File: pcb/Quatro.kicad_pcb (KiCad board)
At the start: 2 copper layers, 100 x 72.8 mm, 97 parts, among them J1 BATTERY, J2 BATTERY, J3 Conn_01x02, J4 UART1 SH, J5 st-link SH, J6 2.54mm 02x03, J7 2.54mm 02x03, Q1 IRLML6402, Q2 IRFML8244, Q3 BSS138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

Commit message: 再発注用に変更
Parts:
- added R30: 10k, Resistor_SMD:R_0603_1608Metric_Pad0.98x0.95mm_HandSolder, F.Cu at (117.8, 109.3)
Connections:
- C10 pad 1: BUTTON -> +3V3
- C17 pad 1: BUTTON -> +3V3
- C18 pad 1: BUTTON -> +3V3
- C19 pad 1: BUTTON -> +3V3
- C20 pad 1: BUTTON -> +3V3
- C22 pad 1: BUTTON -> +3V3
- C6 pad 1: BUTTON -> +3V3
- C7 pad 1: BUTTON -> +3V3
- R14 pad 1: BUTTON -> +3V3
- SP1 pad 1: BUTTON -> +3V3
- U2 pad 3: BUTTON -> +3V3
- U6 pad 13: BUTTON -> +3V3
- U6 pad 8: BUTTON -> +3V3
- U7 pad 1: BUTTON -> +3V3
- U7 pad 19: BUTTON -> +3V3
- U7 pad 32: BUTTON -> +3V3
- U7 pad 48: BUTTON -> +3V3
- U7 pad 64: BUTTON -> +3V3
- U8 pad 12: BUTTON -> +3V3
- U9 pad 12: BUTTON -> +3V3
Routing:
- net BUTTON: track 289.1 -> 52.1 mm, vias 13 -> 2
- net +3V3: track 0.00 -> 198.1 mm, vias 0 -> 5
- net +5V: track 213.8 -> 123.8 mm
- net +3.3VADC: track 205.2 -> 145.2 mm, vias 4 -> 0
- net Net-(R13-Pad1): track 50.9 -> 3.43 mm
- net GND: track 669.4 -> 626.4 mm, vias 51 -> 36
- net TIM5_CH4_MOTOR_R_IN2: track 31.3 -> 66.4 mm, vias 4 -> 3
- net TIM3_CH1_ENC_L_A: track 44.7 -> 19.7 mm
- net TIM5_CH3_MOTOR_R_IN1: track 27.9 -> 51.8 mm, vias 0 -> 2
- net NRST: track 76.9 -> 54.2 mm, vias 0 -> 3
- net Net-(D7-Pad1): track 55.3 -> 77.9 mm
- net MOTOR_R_OUT1: track 24.5 -> 45.7 mm
- net LED5: track 49.3 -> 29.9 mm
- net LED1: track 64.3 -> 80.9 mm
- net MOTOR_L_OUT1: track 31.4 -> 15.1 mm, vias 1 -> 0
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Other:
- board text added: "2021-12-05"
- board text added: "T.Reiji Quatro"
- board text removed: "2021-11-24"
- board text removed: "Quatro Cheese"

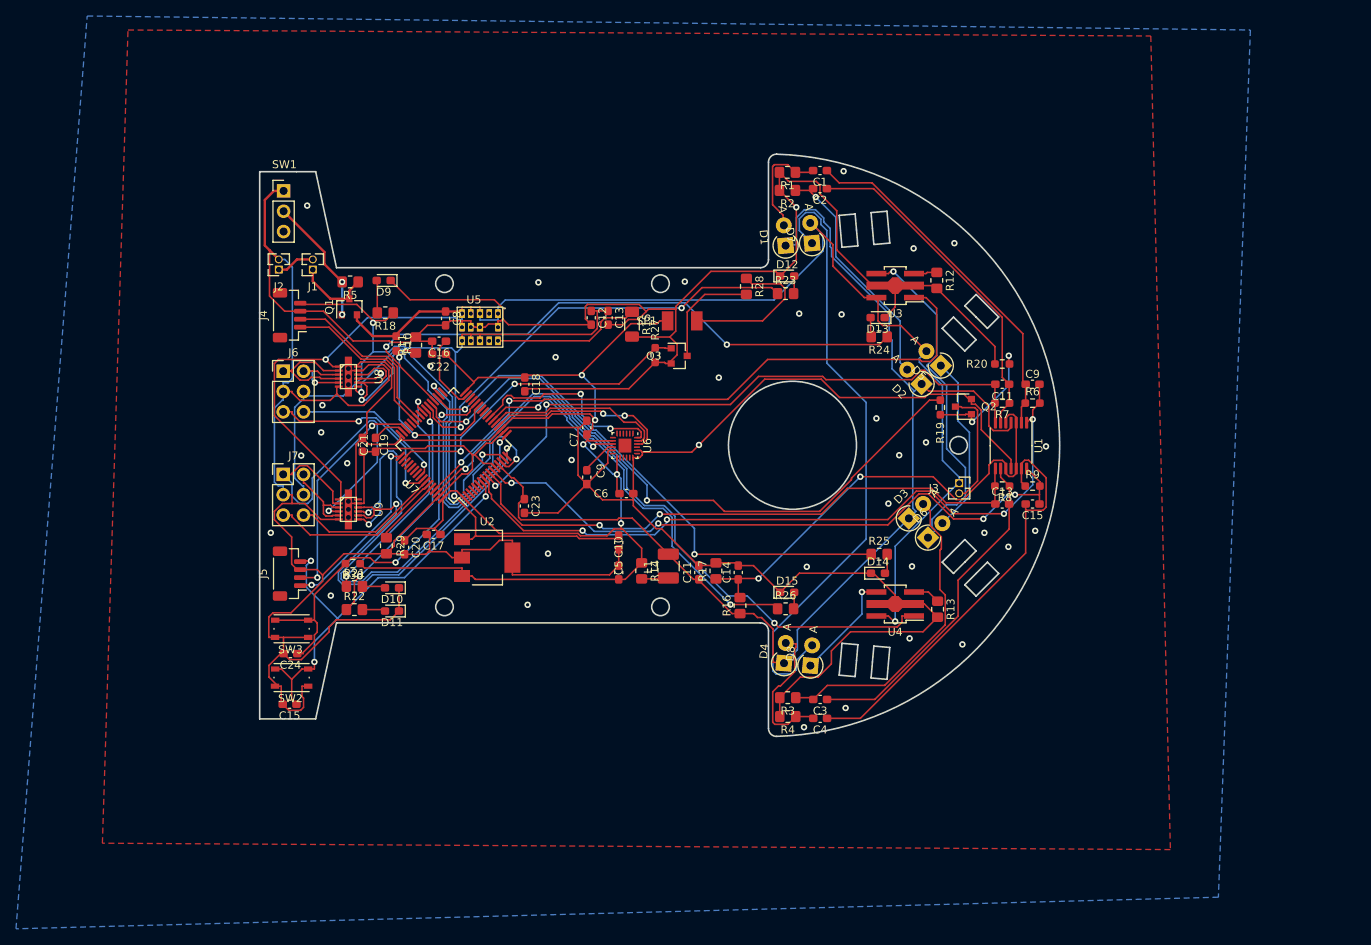
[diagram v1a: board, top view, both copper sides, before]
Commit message: 回路を修正してフットプリントを配置した
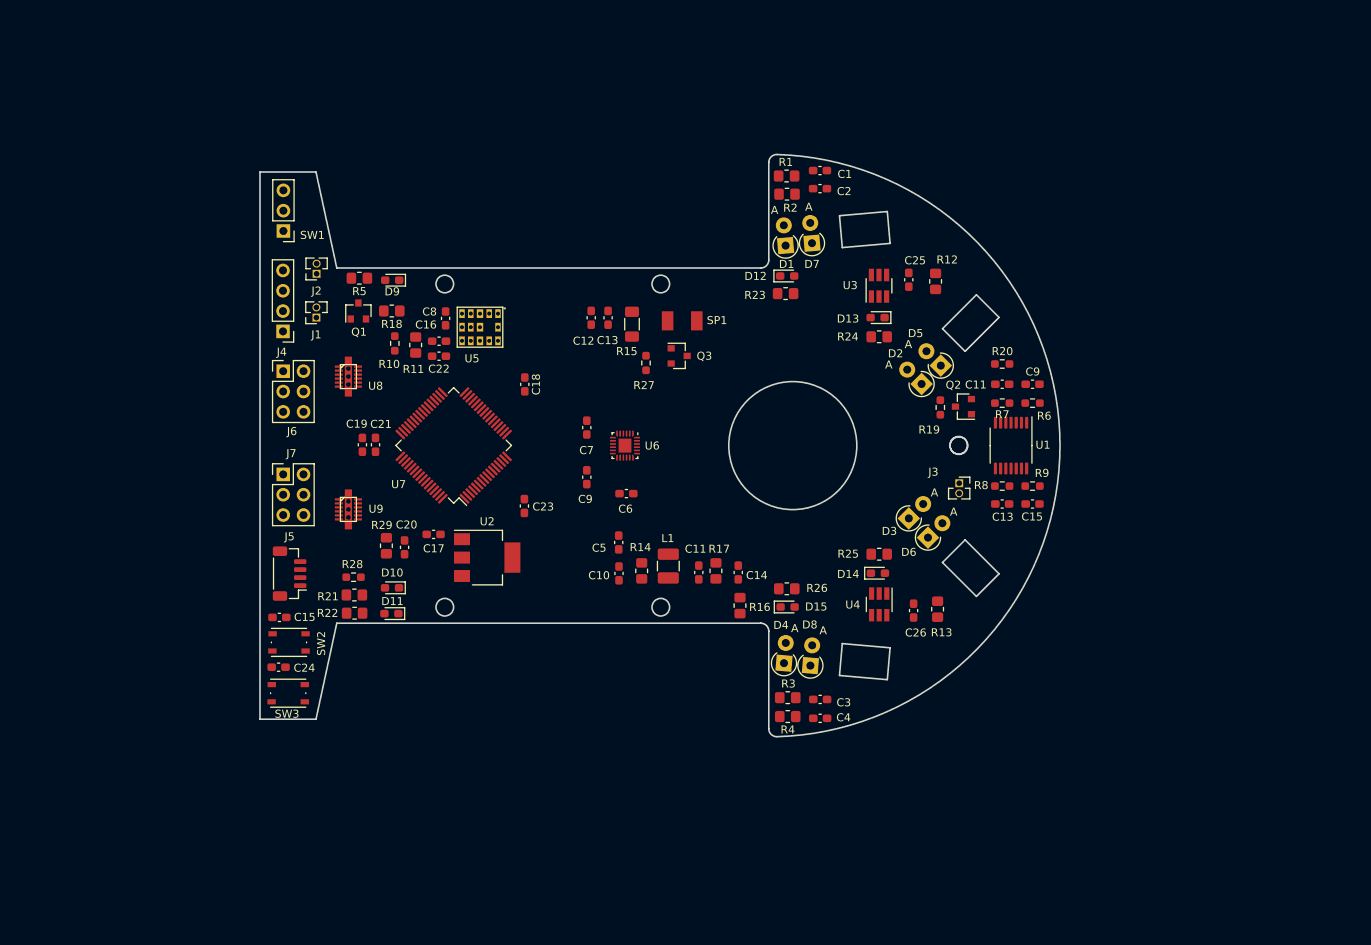
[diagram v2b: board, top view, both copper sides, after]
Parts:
- removed the R28 at (167.0, 74.7)
- added C25: 0.1u, Capacitor_SMD:C_0603_1608Metric_Pad1.08x0.95mm_HandSolder, F.Cu at (187.3, 73.9)
- added C26: 0.1u, Capacitor_SMD:C_0603_1608Metric_Pad1.08x0.95mm_HandSolder, F.Cu at (187.9, 115.2)
- J4: footprint Connector_JST:JST_SH_BM04B-SRSS-TB_1x04-1MP_P1.00mm_Vertical -> Connector_PinHeader_2.54mm:PinHeader_1x04_P2.54mm_Vertical
- R12, R13: value 1 -> 2
- U3, U4: value NJW4616 -> NJU6080; footprint Package_TO_SOT_SMD:SOT-89-5_Handsoldering -> Package_TO_SOT_SMD:SOT-23-6_Handsoldering
- moved C15 10.9 mm to (108.6, 116.1)
- moved SW3 8.06 mm to (109.7, 125.5)
- moved J1 6.02 mm to (113.2, 78.6)
- moved SW1 5.01 mm to (109.1, 67.8), turned to 180 degrees
- moved J2 4.75 mm to (113.3, 73.1)
- moved SW2 4.41 mm to (109.8, 119.2)
- moved R26 2.50 mm to (172.1, 112.5)
- moved C24 2.25 mm to (108.5, 122.3)
- moved J4 2.19 mm to (109.1, 80.3), turned to 180 degrees
- moved U3 2.03 mm to (183.6, 74.6), turned to 90 degrees
- moved U4 2.00 mm to (183.6, 114.5), turned to -90 degrees
- moved D15 1.84 mm to (172.2, 114.8)
- moved R28 1.70 mm to (117.9, 111.0)
- moved R27 1.52 mm to (154.4, 84.3)
- moved Q1 1.25 mm to (118.5, 77.8)
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- renumbered R30 to R28
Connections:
- C10 pad 1: +3V3 -> +3.3V
- C17 pad 1: +3V3 -> +3.3V
- C18 pad 1: +3V3 -> +3.3V
- C19 pad 1: +3V3 -> +3.3V
- C20 pad 1: +3V3 -> +3.3V
- C22 pad 1: +3V3 -> +3.3V
- C6 pad 1: +3V3 -> +3.3V
- C7 pad 1: +3V3 -> +3.3V
- D5 pad 2: +BATT -> +5V
- D7 pad 2: +BATT -> +5V
- J4 pad 4: +5V -> +3.3V
- Q1 pad 2: +BATT -> Net-(J1-Pad1)
- Q1 pad 3: Net-(J1-Pad1) -> +BATT
- R14 pad 1: +3V3 -> +3.3V
- R28 pad 1: +3V3 -> +3.3V
- SP1 pad 1: +3V3 -> +3.3V
- SP1 pad 2: Net-(R28-Pad1) -> Net-(Q3-Pad3)
- SW1 pad 3: Net-(SW1-Pad3) -> unconnected-(SW1-Pad3)
- U2 pad 3: +3V3 -> +3.3V
- U3 pad 5: +BATT -> +5V
- U4 pad 5: +BATT -> +5V
- U5 pad 10: Net-(U5-Pad10) -> unconnected-(U5-Pad10)
- U5 pad 2: Net-(U5-Pad2) -> unconnected-(U5-Pad2)
- U6 pad 12: Net-(U6-Pad12) -> unconnected-(U6-Pad12)
- U6 pad 13: +3V3 -> +3.3V
- U6 pad 21: Net-(U6-Pad21) -> unconnected-(U6-Pad21)
- U6 pad 7: Net-(U6-Pad7) -> unconnected-(U6-Pad7)
- U6 pad 8: +3V3 -> +3.3V
- U7 pad 1: +3V3 -> +3.3V
- U7 pad 19: +3V3 -> +3.3V
- U7 pad 2: Net-(U7-Pad2) -> unconnected-(U7-Pad2)
- U7 pad 24: Net-(U7-Pad24) -> unconnected-(U7-Pad24)
- U7 pad 25: Net-(U7-Pad25) -> unconnected-(U7-Pad25)
- U7 pad 26: Net-(U7-Pad26) -> unconnected-(U7-Pad26)
- U7 pad 28: BUTTON -> unconnected-(U7-Pad28)
- U7 pad 29: Net-(U7-Pad29) -> unconnected-(U7-Pad29)
- U7 pad 3: Net-(U7-Pad3) -> unconnected-(U7-Pad3)
- U7 pad 30: Net-(U7-Pad30) -> unconnected-(U7-Pad30)
- U7 pad 32: +3V3 -> +3.3V
- U7 pad 33: Net-(U7-Pad33) -> unconnected-(U7-Pad33)
- U7 pad 4: Net-(U7-Pad4) -> unconnected-(U7-Pad4)
- U7 pad 41: Net-(U7-Pad41) -> unconnected-(U7-Pad41)
- U7 pad 44: Net-(U7-Pad44) -> unconnected-(U7-Pad44)
- U7 pad 45: Net-(U7-Pad45) -> unconnected-(U7-Pad45)
- U7 pad 48: +3V3 -> +3.3V
- U7 pad 5: Net-(U7-Pad5) -> unconnected-(U7-Pad5)
- U7 pad 51: Net-(U7-Pad51) -> unconnected-(U7-Pad51)
- U7 pad 52: Net-(U7-Pad52) -> unconnected-(U7-Pad52)
- U7 pad 53: Net-(U7-Pad53) -> unconnected-(U7-Pad53)
- U7 pad 54: Net-(U7-Pad54) -> unconnected-(U7-Pad54)
- U7 pad 55: Net-(U7-Pad55) -> unconnected-(U7-Pad55)
- U7 pad 6: Net-(U7-Pad6) -> unconnected-(U7-Pad6)
- U7 pad 64: +3V3 -> +3.3V
- U8 pad 12: +3V3 -> +3.3V
- U9 pad 12: +3V3 -> +3.3V
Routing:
- net GND: track 626.4 -> 0.00 mm, vias 36 -> 0
- net +3V3: track 198.1 -> 0.00 mm, vias 5 -> 0
- net +BATT: track 189.6 -> 0.00 mm, vias 2 -> 0
- net +3.3VADC: track 145.2 -> 0.00 mm
- net +5V: track 123.8 -> 0.00 mm, vias 2 -> 0
- net IR_BL: track 91.4 -> 0.00 mm, vias 4 -> 0
- net TIM11_CH1_IR_LED_OUTER: track 81.9 -> 0.00 mm, vias 2 -> 0
- net TIM8_CH1_MOTOR_FAN: track 81.5 -> 0.00 mm, vias 2 -> 0
- net IR_BR: track 81.3 -> 0.00 mm, vias 4 -> 0
- net LED1: track 80.9 -> 0.00 mm, vias 2 -> 0
- net TIM10_CH1_IR_LED_INNER: track 80.3 -> 0.00 mm, vias 2 -> 0
- net IR_FL: track 78.4 -> 0.00 mm, vias 2 -> 0
- net Net-(D7-Pad1): track 77.9 -> 0.00 mm
- net LED3: track 76.7 -> 0.00 mm, vias 2 -> 0
- net IR_FR: track 74.7 -> 0.00 mm, vias 2 -> 0
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- removed copper zone on B.Cu, net GND
- removed copper zone on F.Cu, net GND
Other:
- outline, holes or cut-outs redrawn
- net class Default removed
- net class Power removed

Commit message: pcb作成して発注
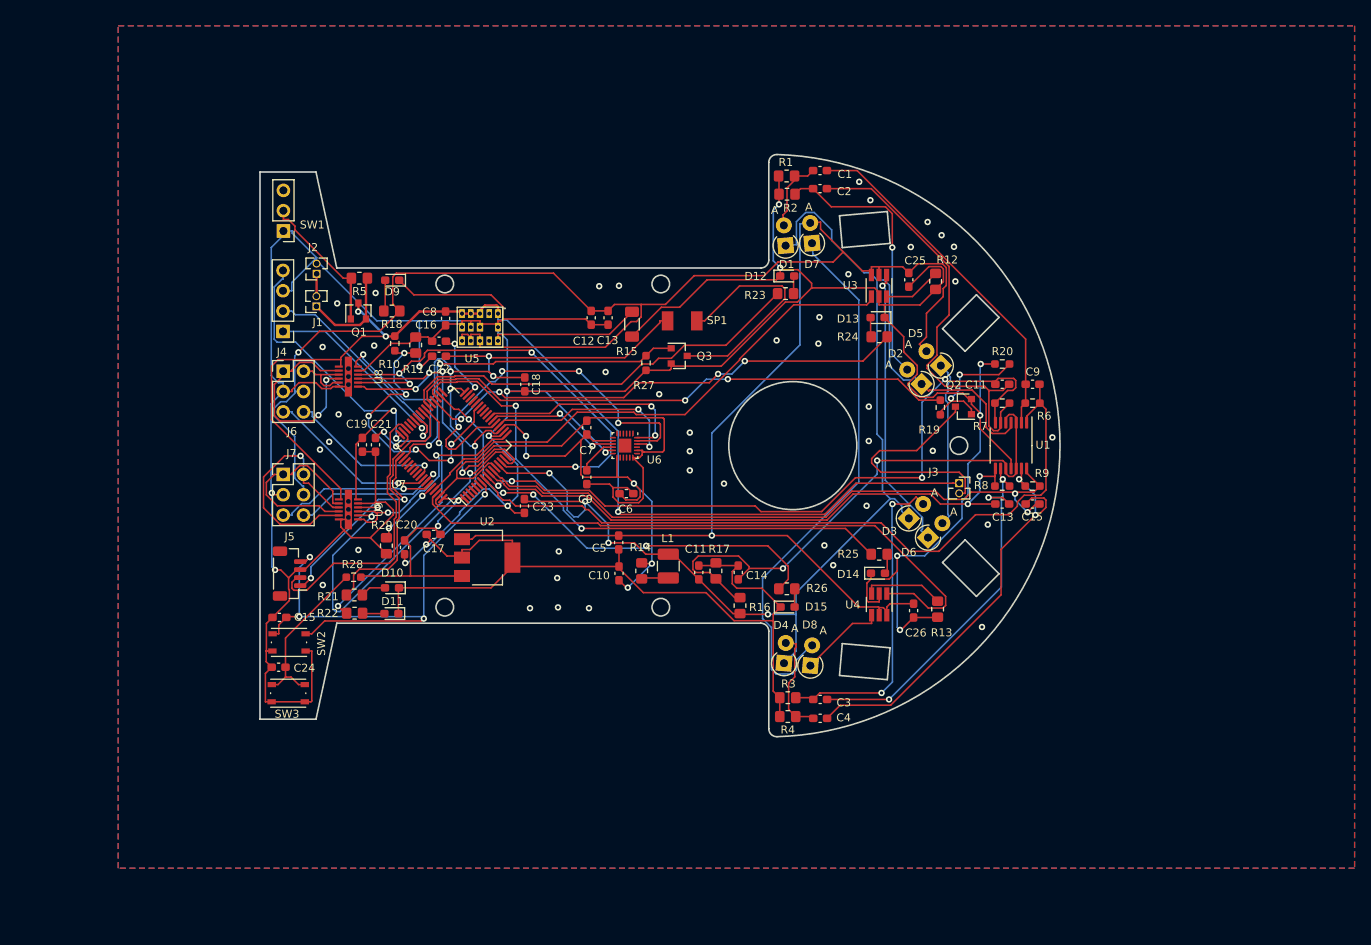
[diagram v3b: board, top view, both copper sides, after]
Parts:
- U8, U9: footprint My_Device:DRV8835 -> Quatro:DRV8835
- moved J1 1.40 mm to (113.2, 77.2)
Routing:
- net GND: track 0.00 -> 670.1 mm, vias 0 -> 57
- net +5V: track 0.00 -> 274.9 mm, vias 0 -> 2
- net +3.3V: track 0.00 -> 229.3 mm, vias 0 -> 15
- net +3.3VADC: track 0.00 -> 168.1 mm, vias 0 -> 4
- net +BATT: track 0.00 -> 135.9 mm, vias 0 -> 3
- net IR_BL: track 0.00 -> 94.3 mm
- net IR_FL: track 0.00 -> 88.3 mm, vias 0 -> 4
- net IR_BR: track 0.00 -> 81.3 mm, vias 0 -> 2
- net TIM11_CH1_IR_LED_OUTER: track 0.00 -> 79.9 mm
- net IR_FR: track 0.00 -> 75.7 mm, vias 0 -> 2
- net TIM8_CH1_MOTOR_FAN: track 0.00 -> 69.8 mm, vias 0 -> 2
- net LED2: track 0.00 -> 69.5 mm, vias 0 -> 2
- net /1.65VA: track 0.00 -> 69.3 mm, vias 0 -> 2
- net Net-(D7-Pad1): track 0.00 -> 68.6 mm
- net NRST: track 0.00 -> 66.0 mm, vias 0 -> 4
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- added copper zone on B.Cu, net GND
- added copper zone on F.Cu, net GND
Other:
- outline, holes or cut-outs redrawn
- board text added: "2022-09-24"
- board text added: "R.Terunuma Piplup"
- board text removed: "2021-12-05"
- board text removed: "T.Reiji Quatro"
